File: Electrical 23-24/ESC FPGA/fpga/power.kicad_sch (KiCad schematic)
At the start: 1 part, among them U1 XC6SLX4-TQG144

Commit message: idk but something
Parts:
- added C1, C10, C11, C12, C3, C4, C6, C7, C8, C9: 4u7, symbol Device:C
- added C13, C5: u47, symbol Device:C
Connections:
- net GND: now reaches U1.108 (GND)
- net GND: now also U1.113 (GND), U1.13 (GND), U1.130 (GND), U1.136 (GND), U1.25 (GND), U1.3 (GND), U1.49 (GND), U1.54 (GND), U1.68 (GND), U1.77 (GND), U1.91 (GND), U1.96 (GND), C1.2, C10.2, C11.2, C12.2, C13.2, C3.2, C4.2, C5.2, C6.2, C7.2, C8.2, C9.2
- net VCC_INT: now reaches U1.128 (VCCINT)
- net VCC_INT: now also U1.19 (VCCINT), U1.28 (VCCINT), U1.52 (VCCINT), U1.89 (VCCINT), C1.1, C3.1, C4.1, C5.1
- net VCC_AUX: now reaches U1.129 (VCCAUX)
- net VCC_AUX: now also U1.20 (VCCAUX), U1.36 (VCCAUX), U1.53 (VCCAUX), U1.90 (VCCAUX), C10.1, C11.1, C12.1, C13.1, C6.1, C7.1, C8.1, C9.1
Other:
- note added: "1.2V"
- note added: "3.3V VCCO_2 must not be 1.8V"

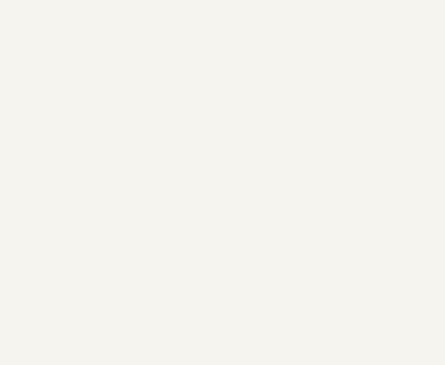
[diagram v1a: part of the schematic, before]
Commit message: Add fpga stuff and stencils
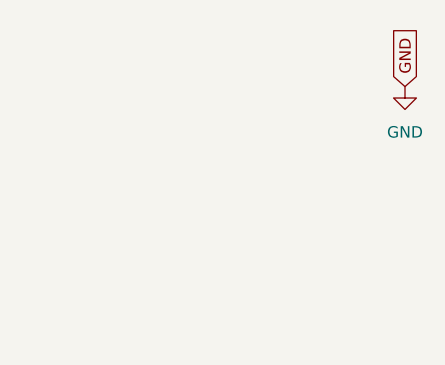
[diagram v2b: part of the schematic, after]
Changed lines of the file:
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@@
+    )
+  )
+  (global_label "GND" (shape input) (at 273.05 27.94 90) (fields_autoplaced)
+    (effects (font (size 1.27 1.27)) (justify left))
+    (property "Intersheetrefs" "${INTERSHEET_REFS}" (at 273.05 21.0843 90)
+      (effects (font (size 1.27 1.27)) (justify left) hide)
     )
   )
@@
         )
       )
+    )
+  )
+  (symbol (lib_id "power:GND") (at 273.05 27.94 0) (unit 1)
+    (in_bom yes) (on_board yes) (dnp no) (fields_autoplaced)
+    (property "Reference" "#PWR040" (at 273.05 34.29 0)
+      (effects (font (size 1.27 1.27)) hide)
+    )
+    (property "Value" "GND" (at 273.05 33.02 0)
+      (effects (font (size 1.27 1.27)))
+    )
+    (property "Footprint" "" (at 273.05 27.94 0)
+      (effects (font (size 1.27 1.27)) hide)
+    )
+    (property "Datasheet" "" (at 273.05 27.94 0)
+      (effects (font (size 1.27 1.27)) hide)
+    )
+    (pin "1")
+    (instances
+      (project "fpga"
+        (path "/5bf59577-a814-4364-8f7a-37815cfb5474/3e04db34-3f8a-4742-be82-6fa24c009343"
+          (reference "#PWR040") (unit 1)
+        )
+        (path "/5bf59577-a814-4364-8f7a-37815cfb5474/1f83b38b-56ef-4110-879b-13379f9dd920"
+          (reference "#PWR026") (unit 1)
+        )
+        (path "/5bf59577-a814-4364-8f7a-37815cfb5474/a286b274-4434-47ab-983d-e64806fdcbd6"
+          (reference "#PWR036") (unit 1)
+        )
+      )

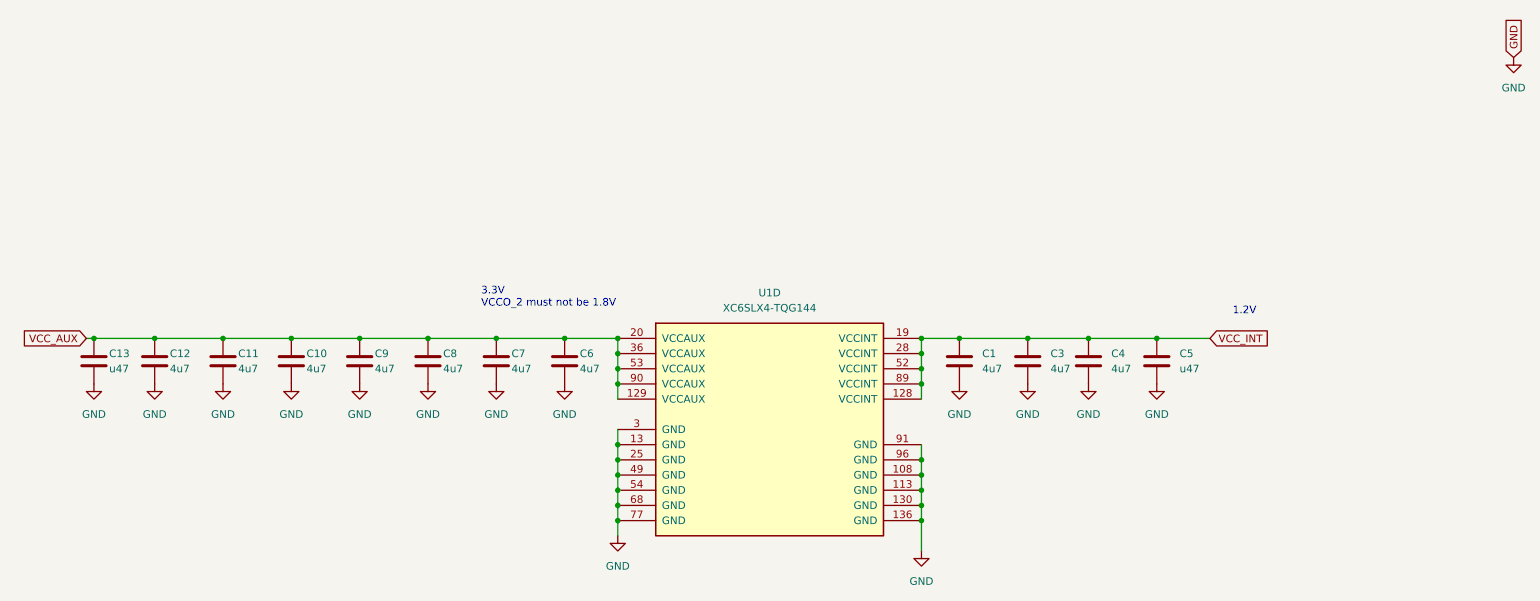
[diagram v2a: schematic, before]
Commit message: Made BOM, need to modify footprints
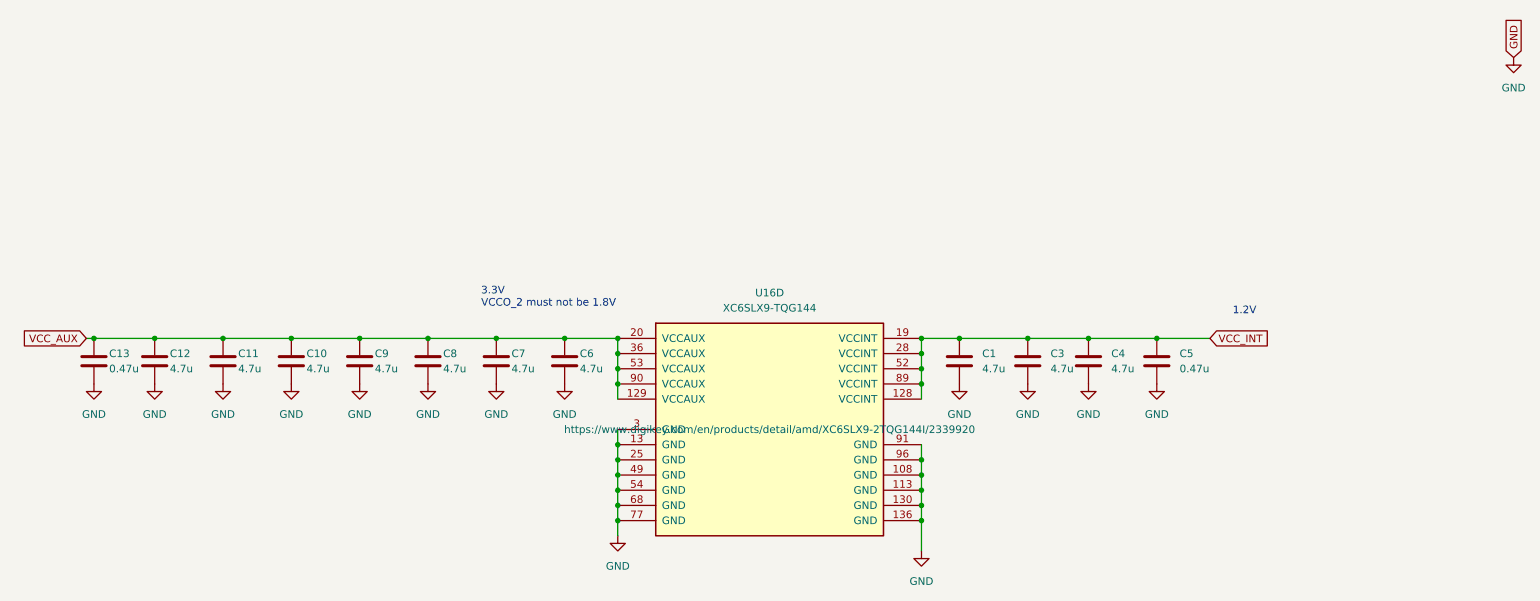
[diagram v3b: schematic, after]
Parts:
- removed U1: XC6SLX4-TQG144, symbol FPGA_Xilinx_Spartan6:XC6SLX4-TQG144
- added U16: XC6SLX9-TQG144, fpga:TQFP-144_20x20mm_P0.5mm, symbol FPGA_Xilinx_Spartan6:XC6SLX9-TQG144
- C1, C10, C11, C12, C3, C4, C6, C7, C8, C9: value 4u7 -> 4.7u; footprint (none) -> Capacitor_SMD:C_0402_1005Metric_Pad0.74x0.62mm_HandSolder
- C13, C5: value u47 -> 0.47u; footprint (none) -> Capacitor_SMD:C_0402_1005Metric_Pad0.74x0.62mm_HandSolder
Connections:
- net GND: now also U16.108 (GND), U16.113 (GND), U16.13 (GND), U16.130 (GND), U16.136 (GND), U16.25 (GND), U16.3 (GND), U16.49 (GND), U16.54 (GND), U16.68 (GND), U16.77 (GND), U16.91 (GND), U16.96 (GND)
- net VCC_AUX: now also U16.129 (VCCAUX), U16.20 (VCCAUX), U16.36 (VCCAUX), U16.53 (VCCAUX), U16.90 (VCCAUX)
- net VCC_INT: now also U16.128 (VCCINT), U16.19 (VCCINT), U16.28 (VCCINT), U16.52 (VCCINT), U16.89 (VCCINT)
